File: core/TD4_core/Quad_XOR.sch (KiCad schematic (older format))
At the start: 2 parts, among them U2 74HC86

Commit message: Decoder done (finally!)
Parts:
- renumbered C1 to C16, U2 to U16

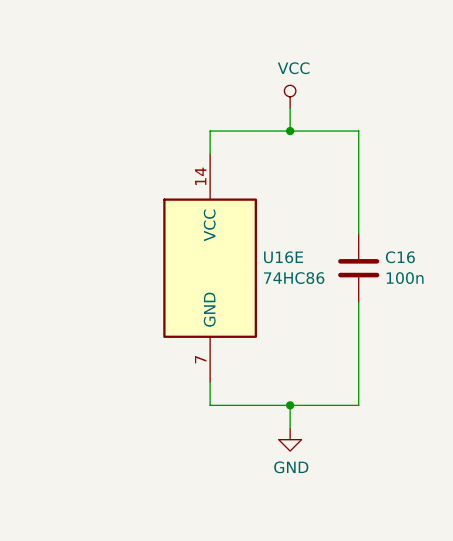
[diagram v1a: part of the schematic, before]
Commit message: Core schematic done. Backplane connector added, including separate .sch file to append.
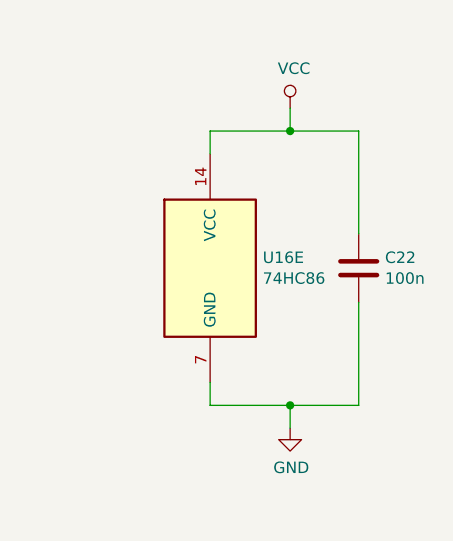
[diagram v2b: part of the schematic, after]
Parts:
- C22: renamed from C16; footprint (none) -> Capacitor_SMD:C_0805_2012Metric
- U16: footprint (none) -> Package_SO:SOIC-14_3.9x8.7mm_P1.27mm
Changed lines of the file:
@@
 encoding utf-8
 Sheet 5 23
-Title "TD4 RAM module"
+Title "TD4 core module"
 Date ""
 Rev "v1.0"
@@
 F 0 "U16" H 4850 2925 50  0000 C CNN
 F 1 "74HC86" H 4850 2834 50  0000 C CNN
-F 2 "" H 4850 2600 50  0001 C CNN
+F 2 "Package_SO:SOIC-14_3.9x8.7mm_P1.27mm" H 4850 2600 50  0001 C CNN
 F 3 "http://www.ti.com/lit/gpn/sn74HC86" H 4850 2600 50  0001 C CNN
 	1    4850 2600
@@
 F 0 "U16" H 4850 3475 50  0000 C CNN
 F 1 "74HC86" H 4850 3384 50  0000 C CNN
-F 2 "" H 4850 3150 50  0001 C CNN
+F 2 "Package_SO:SOIC-14_3.9x8.7mm_P1.27mm" H 4850 3150 50  0001 C CNN
 F 3 "http://www.ti.com/lit/gpn/sn74HC86" H 4850 3150 50  0001 C CNN
 	2    4850 3150
@@
 F 0 "U16" H 4850 4025 50  0000 C CNN
 F 1 "74HC86" H 4850 3934 50  0000 C CNN
-F 2 "" H 4850 3700 50  0001 C CNN
+F 2 "Package_SO:SOIC-14_3.9x8.7mm_P1.27mm" H 4850 3700 50  0001 C CNN
 F 3 "http://www.ti.com/lit/gpn/sn74HC86" H 4850 3700 50  0001 C CNN
 	3    4850 3700
@@
 F 0 "U16" H 4850 4575 50  0000 C CNN
 F 1 "74HC86" H 4850 4484 50  0000 C CNN
-F 2 "" H 4850 4250 50  0001 C CNN
+F 2 "Package_SO:SOIC-14_3.9x8.7mm_P1.27mm" H 4850 4250 50  0001 C CNN
 F 3 "http://www.ti.com/lit/gpn/sn74HC86" H 4850 4250 50  0001 C CNN
 	4    4850 4250
@@
 F 0 "U16" H 7330 3246 50  0000 L CNN
 F 1 "74HC86" H 7330 3155 50  0000 L CNN
-F 2 "" H 7100 3200 50  0001 C CNN
+F 2 "Package_SO:SOIC-14_3.9x8.7mm_P1.27mm" H 7100 3200 50  0001 C CNN
 F 3 "http://www.ti.com/lit/gpn/sn74HC86" H 7100 3200 50  0001 C CNN
 	5    7100 3200
@@
 AR Path="/5C5DC05E/5CCDF31F/5C5DC564" Ref="C?"  Part="1"
 AR Path="/5C5DC05E/5CCE6007/5C5DC564" Ref="C?"  Part="1"
-AR Path="/5C594F41/5C666CBD/5C5DC564" Ref="C16"  Part="1"
+AR Path="/5C594F41/5C666CBD/5C5DC564" Ref="C22"  Part="1"
 AR Path="/5C594F41/5C66DBDC/5C5DC564" Ref="C?"  Part="1"
-AR Path="/5C594F41/5C66DBF1/5C5DC564" Ref="C19"  Part="1"
-AR Path="/5C594F41/5C66DC06/5C5DC564" Ref="C21"  Part="1"
-AR Path="/5C594F41/5C66DC24/5C5DC564" Ref="C23"  Part="1"
-AR Path="/5C594F41/5C675207/5C5DC564" Ref="C26"  Part="1"
-F 0 "C16" H 7865 3246 50  0000 L CNN
+AR Path="/5C594F41/5C66DBF1/5C5DC564" Ref="C25"  Part="1"
+AR Path="/5C594F41/5C66DC06/5C5DC564" Ref="C27"  Part="1"
+AR Path="/5C594F41/5C66DC24/5C5DC564" Ref="C29"  Part="1"
+AR Path="/5C594F41/5C675207/5C5DC564" Ref="C32"  Part="1"
+F 0 "C22" H 7865 3246 50  0000 L CNN
 F 1 "100n" H 7865 3155 50  0000 L CNN
-F 2 "" H 7788 3050 50  0001 C CNN
+F 2 "Capacitor_SMD:C_0805_2012Metric" H 7788 3050 50  0001 C CNN
 F 3 "~" H 7750 3200 50  0001 C CNN
 	1    7750 3200
@@
 AR Path="/5C5DC05E/5CCDF31F/5C5DF5EB" Ref="#PWR?"  Part="1"
 AR Path="/5C5DC05E/5CCE6007/5C5DF5EB" Ref="#PWR?"  Part="1"
-AR Path="/5C594F41/5C666CBD/5C5DF5EB" Ref="#PWR056"  Part="1"
+AR Path="/5C594F41/5C666CBD/5C5DF5EB" Ref="#PWR070"  Part="1"
 AR Path="/5C594F41/5C66DBDC/5C5DF5EB" Ref="#PWR?"  Part="1"
-AR Path="/5C594F41/5C66DBF1/5C5DF5EB" Ref="#PWR064"  Part="1"
-AR Path="/5C594F41/5C66DC06/5C5DF5EB" Ref="#PWR070"  Part="1"
-AR Path="/5C594F41/5C66DC24/5C5DF5EB" Ref="#PWR076"  Part="1"
-AR Path="/5C594F41/5C675207/5C5DF5EB" Ref="#PWR084"  Part="1"
-F 0 "#PWR084" H 7450 3650 50  0001 C CNN
+AR Path="/5C594F41/5C66DBF1/5C5DF5EB" Ref="#PWR078"  Part="1"
+AR Path="/5C594F41/5C66DC06/5C5DF5EB" Ref="#PWR084"  Part="1"
+AR Path="/5C594F41/5C66DC24/5C5DF5EB" Ref="#PWR090"  Part="1"
+AR Path="/5C594F41/5C675207/5C5DF5EB" Ref="#PWR098"  Part="1"
+F 0 "#PWR098" H 7450 3650 50  0001 C CNN
 F 1 "GND" H 7455 3727 50  0000 C CNN
 F 2 "" H 7450 3900 50  0001 C CNN
@@
 AR Path="/5C5DC05E/5CCDF31F/5C5E1083" Ref="#PWR?"  Part="1"
 AR Path="/5C5DC05E/5CCE6007/5C5E1083" Ref="#PWR?"  Part="1"
-AR Path="/5C594F41/5C666CBD/5C5E1083" Ref="#PWR055"  Part="1"
+AR Path="/5C594F41/5C666CBD/5C5E1083" Ref="#PWR069"  Part="1"
 AR Path="/5C594F41/5C66DBDC/5C5E1083" Ref="#PWR?"  Part="1"
-AR Path="/5C594F41/5C66DBF1/5C5E1083" Ref="#PWR063"  Part="1"
-AR Path="/5C594F41/5C66DC06/5C5E1083" Ref="#PWR069"  Part="1"
-AR Path="/5C594F41/5C66DC24/5C5E1083" Ref="#PWR075"  Part="1"
-AR Path="/5C594F41/5C675207/5C5E1083" Ref="#PWR083"  Part="1"
-F 0 "#PWR083" H 7450 2350 50  0001 C CNN
+AR Path="/5C594F41/5C66DBF1/5C5E1083" Ref="#PWR077"  Part="1"
+AR Path="/5C594F41/5C66DC06/5C5E1083" Ref="#PWR083"  Part="1"
+AR Path="/5C594F41/5C66DC24/5C5E1083" Ref="#PWR089"  Part="1"
+AR Path="/5C594F41/5C675207/5C5E1083" Ref="#PWR097"  Part="1"
+F 0 "#PWR097" H 7450 2350 50  0001 C CNN
 F 1 "VCC" H 7467 2673 50  0000 C CNN
 F 2 "" H 7450 2500 50  0001 C CNN

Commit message: Fixed minor core PCB errors
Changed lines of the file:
@@
 AR Path="/5C594F41/5C66DC24/5C5DC2EE" Ref="U23"  Part="1"
 AR Path="/5C594F41/5C675207/5C5DC2EE" Ref="U26"  Part="1"
-F 0 "U16" H 4850 2925 50  0000 C CNN
+F 0 "U26" H 4850 2925 50  0000 C CNN
 F 1 "74HC86" H 4850 2834 50  0000 C CNN
 F 2 "Package_SO:SOIC-14_3.9x8.7mm_P1.27mm" H 4850 2600 50  0001 C CNN
@@
 AR Path="/5C594F41/5C66DC24/5C5DC376" Ref="U23"  Part="2"
 AR Path="/5C594F41/5C675207/5C5DC376" Ref="U26"  Part="2"
-F 0 "U16" H 4850 3475 50  0000 C CNN
+F 0 "U26" H 4850 3475 50  0000 C CNN
 F 1 "74HC86" H 4850 3384 50  0000 C CNN
 F 2 "Package_SO:SOIC-14_3.9x8.7mm_P1.27mm" H 4850 3150 50  0001 C CNN
@@
 AR Path="/5C594F41/5C66DC24/5C5DC396" Ref="U23"  Part="3"
 AR Path="/5C594F41/5C675207/5C5DC396" Ref="U26"  Part="3"
-F 0 "U16" H 4850 4025 50  0000 C CNN
+F 0 "U26" H 4850 4025 50  0000 C CNN
 F 1 "74HC86" H 4850 3934 50  0000 C CNN
 F 2 "Package_SO:SOIC-14_3.9x8.7mm_P1.27mm" H 4850 3700 50  0001 C CNN
@@
 AR Path="/5C594F41/5C66DC24/5C5DC3D2" Ref="U23"  Part="4"
 AR Path="/5C594F41/5C675207/5C5DC3D2" Ref="U26"  Part="4"
-F 0 "U16" H 4850 4575 50  0000 C CNN
+F 0 "U26" H 4850 4575 50  0000 C CNN
 F 1 "74HC86" H 4850 4484 50  0000 C CNN
 F 2 "Package_SO:SOIC-14_3.9x8.7mm_P1.27mm" H 4850 4250 50  0001 C CNN
@@
 AR Path="/5C594F41/5C66DC24/5C5DC430" Ref="U23"  Part="5"
 AR Path="/5C594F41/5C675207/5C5DC430" Ref="U26"  Part="5"
-F 0 "U16" H 7330 3246 50  0000 L CNN
+F 0 "U26" H 7330 3246 50  0000 L CNN
 F 1 "74HC86" H 7330 3155 50  0000 L CNN
 F 2 "Package_SO:SOIC-14_3.9x8.7mm_P1.27mm" H 7100 3200 50  0001 C CNN
@@
 AR Path="/5C594F41/5C66DC24/5C5DC564" Ref="C29"  Part="1"
 AR Path="/5C594F41/5C675207/5C5DC564" Ref="C32"  Part="1"
-F 0 "C22" H 7865 3246 50  0000 L CNN
+F 0 "C32" H 7865 3246 50  0000 L CNN
 F 1 "100n" H 7865 3155 50  0000 L CNN
 F 2 "Capacitor_SMD:C_0805_2012Metric" H 7788 3050 50  0001 C CNN
@@
 AR Path="/5C5DC05E/5CCDF31F/5C5DF5EB" Ref="#PWR?"  Part="1"
 AR Path="/5C5DC05E/5CCE6007/5C5DF5EB" Ref="#PWR?"  Part="1"
-AR Path="/5C594F41/5C666CBD/5C5DF5EB" Ref="#PWR070"  Part="1"
+AR Path="/5C594F41/5C666CBD/5C5DF5EB" Ref="#PWR072"  Part="1"
 AR Path="/5C594F41/5C66DBDC/5C5DF5EB" Ref="#PWR?"  Part="1"
-AR Path="/5C594F41/5C66DBF1/5C5DF5EB" Ref="#PWR078"  Part="1"
-AR Path="/5C594F41/5C66DC06/5C5DF5EB" Ref="#PWR084"  Part="1"
-AR Path="/5C594F41/5C66DC24/5C5DF5EB" Ref="#PWR090"  Part="1"
-AR Path="/5C594F41/5C675207/5C5DF5EB" Ref="#PWR098"  Part="1"
-F 0 "#PWR098" H 7450 3650 50  0001 C CNN
+AR Path="/5C594F41/5C66DBF1/5C5DF5EB" Ref="#PWR080"  Part="1"
+AR Path="/5C594F41/5C66DC06/5C5DF5EB" Ref="#PWR086"  Part="1"
+AR Path="/5C594F41/5C66DC24/5C5DF5EB" Ref="#PWR092"  Part="1"
+AR Path="/5C594F41/5C675207/5C5DF5EB" Ref="#PWR0100"  Part="1"
+F 0 "#PWR0100" H 7450 3650 50  0001 C CNN
 F 1 "GND" H 7455 3727 50  0000 C CNN
 F 2 "" H 7450 3900 50  0001 C CNN
@@
 AR Path="/5C5DC05E/5CCDF31F/5C5E1083" Ref="#PWR?"  Part="1"
 AR Path="/5C5DC05E/5CCE6007/5C5E1083" Ref="#PWR?"  Part="1"
-AR Path="/5C594F41/5C666CBD/5C5E1083" Ref="#PWR069"  Part="1"
+AR Path="/5C594F41/5C666CBD/5C5E1083" Ref="#PWR071"  Part="1"
 AR Path="/5C594F41/5C66DBDC/5C5E1083" Ref="#PWR?"  Part="1"
-AR Path="/5C594F41/5C66DBF1/5C5E1083" Ref="#PWR077"  Part="1"
-AR Path="/5C594F41/5C66DC06/5C5E1083" Ref="#PWR083"  Part="1"
-AR Path="/5C594F41/5C66DC24/5C5E1083" Ref="#PWR089"  Part="1"
-AR Path="/5C594F41/5C675207/5C5E1083" Ref="#PWR097"  Part="1"
-F 0 "#PWR097" H 7450 2350 50  0001 C CNN
+AR Path="/5C594F41/5C66DBF1/5C5E1083" Ref="#PWR079"  Part="1"
+AR Path="/5C594F41/5C66DC06/5C5E1083" Ref="#PWR085"  Part="1"
+AR Path="/5C594F41/5C66DC24/5C5E1083" Ref="#PWR091"  Part="1"
+AR Path="/5C594F41/5C675207/5C5E1083" Ref="#PWR099"  Part="1"
+F 0 "#PWR099" H 7450 2350 50  0001 C CNN
 F 1 "VCC" H 7467 2673 50  0000 C CNN
 F 2 "" H 7450 2500 50  0001 C CNN

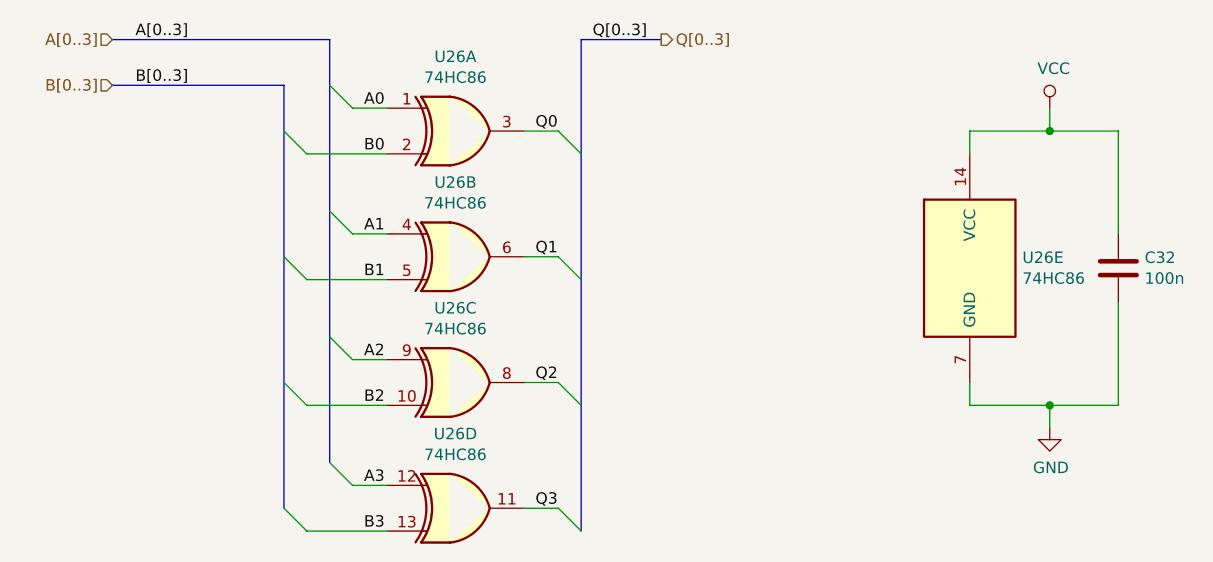
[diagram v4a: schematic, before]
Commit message: Replaced debug headers with vertical ones
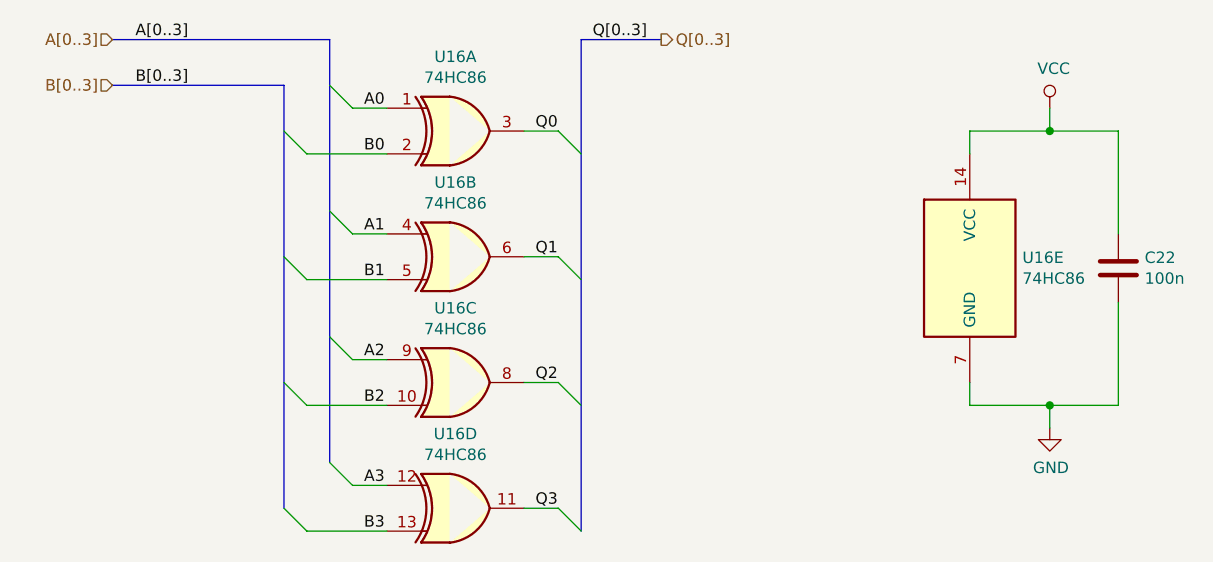
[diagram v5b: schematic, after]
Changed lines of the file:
@@
 AR Path="/5C594F41/5C66DC24/5C5DC2EE" Ref="U23"  Part="1"
 AR Path="/5C594F41/5C675207/5C5DC2EE" Ref="U26"  Part="1"
-F 0 "U26" H 4850 2925 50  0000 C CNN
+F 0 "U16" H 4850 2925 50  0000 C CNN
 F 1 "74HC86" H 4850 2834 50  0000 C CNN
 F 2 "Package_SO:SOIC-14_3.9x8.7mm_P1.27mm" H 4850 2600 50  0001 C CNN
@@
 AR Path="/5C594F41/5C66DC24/5C5DC376" Ref="U23"  Part="2"
 AR Path="/5C594F41/5C675207/5C5DC376" Ref="U26"  Part="2"
-F 0 "U26" H 4850 3475 50  0000 C CNN
+F 0 "U16" H 4850 3475 50  0000 C CNN
 F 1 "74HC86" H 4850 3384 50  0000 C CNN
 F 2 "Package_SO:SOIC-14_3.9x8.7mm_P1.27mm" H 4850 3150 50  0001 C CNN
@@
 AR Path="/5C594F41/5C66DC24/5C5DC396" Ref="U23"  Part="3"
 AR Path="/5C594F41/5C675207/5C5DC396" Ref="U26"  Part="3"
-F 0 "U26" H 4850 4025 50  0000 C CNN
+F 0 "U16" H 4850 4025 50  0000 C CNN
 F 1 "74HC86" H 4850 3934 50  0000 C CNN
 F 2 "Package_SO:SOIC-14_3.9x8.7mm_P1.27mm" H 4850 3700 50  0001 C CNN
@@
 AR Path="/5C594F41/5C66DC24/5C5DC3D2" Ref="U23"  Part="4"
 AR Path="/5C594F41/5C675207/5C5DC3D2" Ref="U26"  Part="4"
-F 0 "U26" H 4850 4575 50  0000 C CNN
+F 0 "U16" H 4850 4575 50  0000 C CNN
 F 1 "74HC86" H 4850 4484 50  0000 C CNN
 F 2 "Package_SO:SOIC-14_3.9x8.7mm_P1.27mm" H 4850 4250 50  0001 C CNN
@@
 AR Path="/5C594F41/5C66DC24/5C5DC430" Ref="U23"  Part="5"
 AR Path="/5C594F41/5C675207/5C5DC430" Ref="U26"  Part="5"
-F 0 "U26" H 7330 3246 50  0000 L CNN
+F 0 "U16" H 7330 3246 50  0000 L CNN
 F 1 "74HC86" H 7330 3155 50  0000 L CNN
 F 2 "Package_SO:SOIC-14_3.9x8.7mm_P1.27mm" H 7100 3200 50  0001 C CNN
@@
 AR Path="/5C594F41/5C66DC24/5C5DC564" Ref="C29"  Part="1"
 AR Path="/5C594F41/5C675207/5C5DC564" Ref="C32"  Part="1"
-F 0 "C32" H 7865 3246 50  0000 L CNN
+F 0 "C22" H 7865 3246 50  0000 L CNN
 F 1 "100n" H 7865 3155 50  0000 L CNN
 F 2 "Capacitor_SMD:C_0805_2012Metric" H 7788 3050 50  0001 C CNN
